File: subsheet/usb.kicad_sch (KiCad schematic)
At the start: 8 parts, among them J501 USB_C_Receptacle, U5 FUSB302BMPX, U501 DT1240A-04LP-7

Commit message: Copy in component arrangement from SDMMC test design
Already had an efficient arrangement for the SPI flash chip, Clock
crystal, and Antenna.
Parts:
- renumbered C708 to C501, C708 to C502, C708 to C503, C708 to C504, C302 to C505, U5 to U502
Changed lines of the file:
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@@
   (symbol (lib_id "power:GND") (at 180.34 45.72 0) (mirror y) (unit 1)
     (in_bom yes) (on_board yes) (dnp no) (fields_autoplaced)
-    (property "Reference" "#PWR019" (at 180.34 52.07 0)
+    (property "Reference" "#PWR0510" (at 180.34 52.07 0)
       (effects (font (size 1.27 1.27)) hide)
     )
@@
   (symbol (lib_id "power:GND") (at 129.54 45.72 0) (mirror y) (unit 1)
     (in_bom yes) (on_board yes) (dnp no) (fields_autoplaced)
-    (property "Reference" "#PWR021" (at 129.54 52.07 0)
+    (property "Reference" "#PWR0505" (at 129.54 52.07 0)
       (effects (font (size 1.27 1.27)) hide)
     )
@@
   (symbol (lib_id "Device:C_Small") (at 129.54 43.18 0) (mirror y) (unit 1)
     (in_bom yes) (on_board yes) (dnp no) (fields_autoplaced)
-    (property "Reference" "C708" (at 132.08 41.9163 0)
+    (property "Reference" "C502" (at 132.08 41.9163 0)
       (effects (font (size 1.27 1.27)) (justify right))
     )
@@
   (symbol (lib_id "power:+5V") (at 180.34 38.1 0) (mirror y) (unit 1)
     (in_bom yes) (on_board yes) (dnp no) (fields_autoplaced)
-    (property "Reference" "#PWR020" (at 180.34 41.91 0)
+    (property "Reference" "#PWR0509" (at 180.34 41.91 0)
       (effects (font (size 1.27 1.27)) hide)
     )
@@
   (symbol (lib_id "Device:C_Small") (at 132.08 68.58 0) (mirror y) (unit 1)
     (in_bom yes) (on_board yes) (dnp no) (fields_autoplaced)
-    (property "Reference" "C708" (at 134.62 67.3163 0)
+    (property "Reference" "C503" (at 134.62 67.3163 0)
       (effects (font (size 1.27 1.27)) (justify right))
     )
@@
   (symbol (lib_id "Device:C_Small") (at 167.64 43.18 0) (mirror y) (unit 1)
     (in_bom yes) (on_board yes) (dnp no) (fields_autoplaced)
-    (property "Reference" "C708" (at 170.18 41.9163 0)
+    (property "Reference" "C504" (at 170.18 41.9163 0)
       (effects (font (size 1.27 1.27)) (justify right))
     )
@@
   (symbol (lib_id "Device:C_Small") (at 180.34 43.18 0) (unit 1)
     (in_bom yes) (on_board yes) (dnp no) (fields_autoplaced)
-    (property "Reference" "C302" (at 182.88 41.9163 0)
+    (property "Reference" "C505" (at 182.88 41.9163 0)
       (effects (font (size 1.27 1.27)) (justify left))
     )
@@
   (symbol (lib_id "power:GND") (at 167.64 45.72 0) (mirror y) (unit 1)
     (in_bom yes) (on_board yes) (dnp no) (fields_autoplaced)
-    (property "Reference" "#PWR019" (at 167.64 52.07 0)
+    (property "Reference" "#PWR0508" (at 167.64 52.07 0)
       (effects (font (size 1.27 1.27)) hide)
     )
@@
   (symbol (lib_id "Device:C_Small") (at 119.38 68.58 0) (mirror y) (unit 1)
     (in_bom yes) (on_board yes) (dnp no) (fields_autoplaced)
-    (property "Reference" "C708" (at 121.92 67.3163 0)
+    (property "Reference" "C501" (at 121.92 67.3163 0)
       (effects (font (size 1.27 1.27)) (justify right))
     )
@@
   (symbol (lib_id "Interface_USB:FUSB302BMPX") (at 152.4 58.42 0) (mirror y) (unit 1)
     (in_bom yes) (on_board yes) (dnp no) (fields_autoplaced)
-    (property "Reference" "U5" (at 152.7459 68.58 0)
-      (effects (font (size 1.27 1.27)) (justify right))
-    )
+    (property "Reference" "U502" (at 152.7459 68.58 0)
+      (effects (font (size 1.27 1.27)) (justify right))
+    )

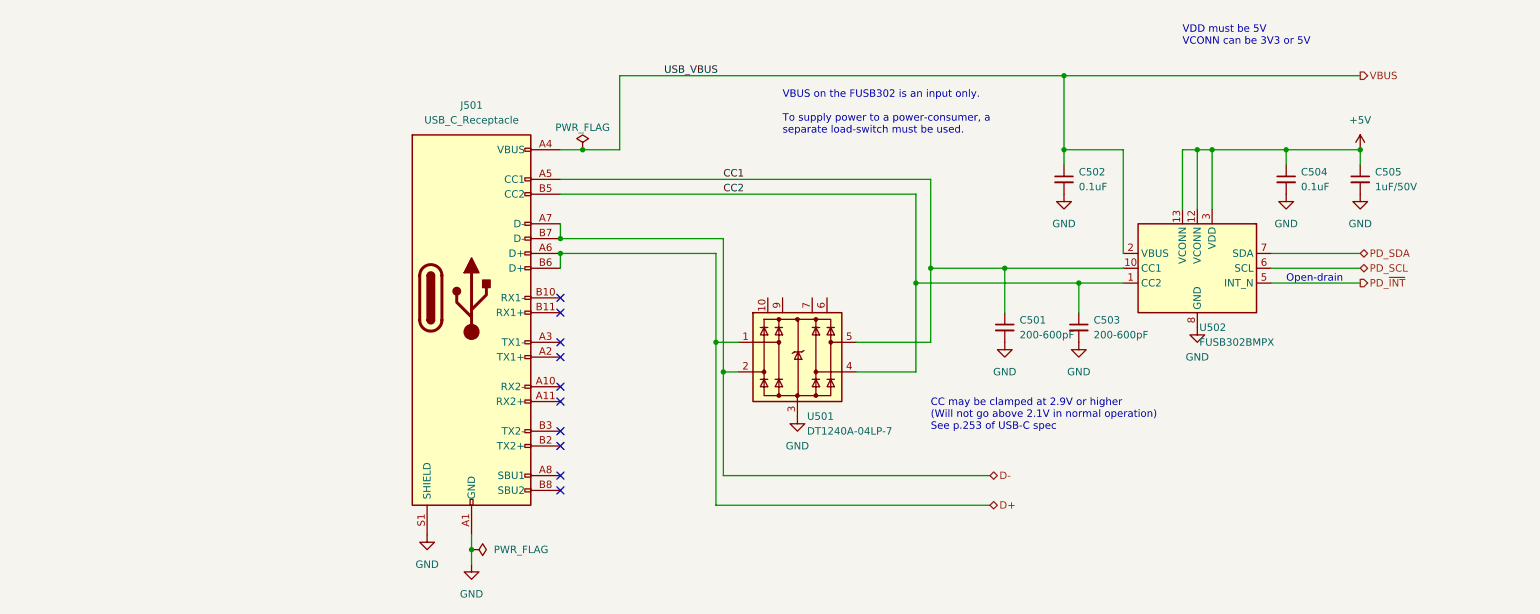
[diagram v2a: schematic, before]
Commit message: Add 5v and 3v3 buck regulators, brige rectifier
Buck regulators are copied from existing designs. 5V regulator needs to
be reworked though; due to ESD vulnerability.

Added 4 diodes in bridge rectifier configuration. Provides a simpler
solution than the polarity-protected eFuse. Due to how the
buck-regulators work, it should be fine for any voltage from ~4.8V 17V
(max Vin of buck regulator). Downside is icnreased power-dissipation,
but since this board is not intended to use a lot of current it should
be good (the USB port can bypass this too, but only for 5V)
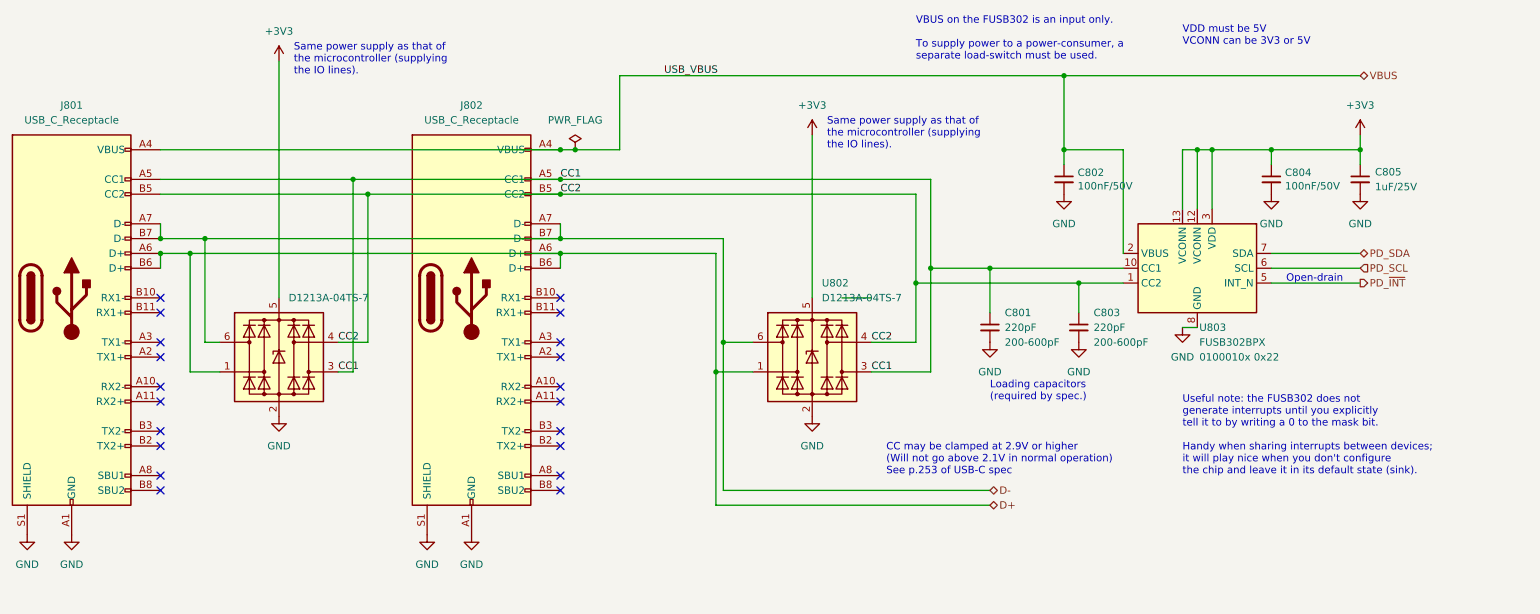
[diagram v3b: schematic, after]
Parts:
- removed C501, C503: 200-600pF, symbol Device:C_Small
- removed C502, C504: 0.1uF, symbol Device:C_Small
- removed C505: 1uF/50V, Capacitor_SMD:C_0805_2012Metric, symbol Device:C_Small
- removed U501: DT1240A-04LP-7, Package_DFN_QFN:Diodes_UDFN-10_1.0x2.5mm_P0.5mm, symbol Power_Protection_custom:DT1240A-04LP-7
- added C801, C803: 220pF, Capacitor_SMD:C_0402_1005Metric, symbol Device:C_Small
- added C802, C804: 100nF/50V, Capacitor_SMD:C_0402_1005Metric, symbol Device:C_Small
- added C805: 1uF/25V, Capacitor_SMD:C_0402_1005Metric, symbol Device:C_Small
- added J801: USB_C_Receptacle, Connector_USB:USB_C_Receptacle_Molex_105450-0101, symbol Connector:USB_C_Receptacle
- added U801, U802: D1213A-04TS-7, Package_TO_SOT_SMD:TSOT-23-6, symbol Power_Protection_custom:D1213A-04TS-7
- U803: renamed from U502; value FUSB302BMPX -> FUSB302BPX; I2C address (none) -> 0100010x 0x22; JLCPCB_CORRECTION (none) -> 0;0;270; LCSC (none) -> C442699
- renumbered J501 to J802
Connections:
- net CC1: now also C801.1, J801.A5 (CC1), U801.3 (I/O2), U802.3 (I/O2)
- net CC2: now also C803.1, J801.B5 (CC2), U801.4 (I/O3), U802.4 (I/O3)
- net D+: now also J801.A6 (D+), J801.B6 (D+), U801.1 (I/O1), U802.1 (I/O1)
- net D-: now also J801.A7 (D-), J801.B7 (D-), U801.6 (I/O4), U802.6 (I/O4)
- net GND: now also C801.2, C802.2, C803.2, C804.2, C805.2, J801.A1 (GND), J801.A12 (GND), J801.B1 (GND), J801.B12 (GND), J801.S1 (SHIELD), U801.2 (GND), U802.2 (GND)
- net VBUS: now also C802.1, J801.A4 (VBUS), J801.A9 (VBUS), J801.B4 (VBUS), J801.B9 (VBUS)
- net +5V renamed +3V3
- net +3V3: now also C804.1, C805.1, U801.5 (VBUS), U802.5 (VBUS)
- no-connect marks 10 -> 20
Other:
- note added: "Loading capacitors (required by spec.)"
- note added: "Same power supply as that of the microcontroller (supplying the IO lines)."
- note added: "Useful note: the FUSB302 does not generate interrupts until you explicitly tell it to by writing a 0 to the mask bit. Handy when sharing interrupts between devices; it will play nice when you don't configure the chip and leave it in its default state (sink)."
- company: (c) Escape This -> copyright Escape This 2024
- title: Environment Controller ESP32-S3-4M -> Puzzle Board

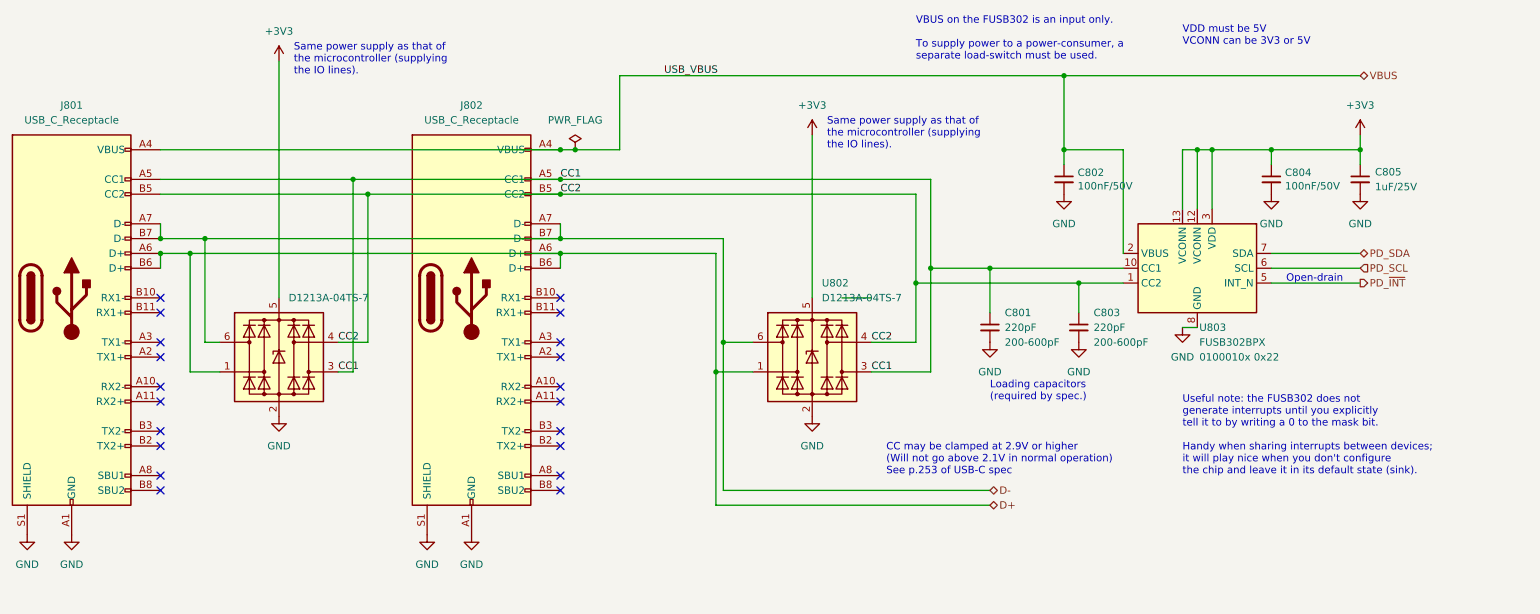
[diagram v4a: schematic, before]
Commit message: Removed USB-PD circuit - simplifies board
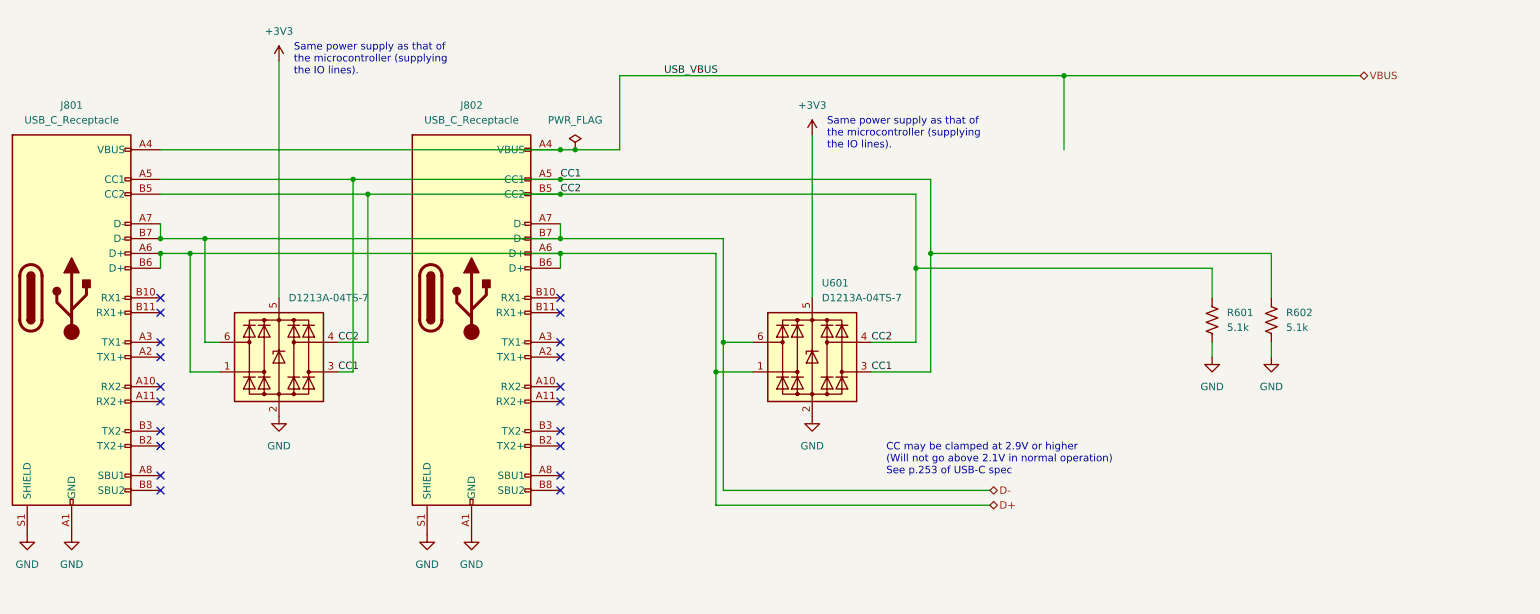
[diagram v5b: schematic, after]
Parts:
- removed C801, C803: 220pF, Capacitor_SMD:C_0402_1005Metric, symbol Device:C_Small
- removed C802, C804: 100nF/50V, Capacitor_SMD:C_0402_1005Metric, symbol Device:C_Small
- removed C805: 1uF/25V, Capacitor_SMD:C_0402_1005Metric, symbol Device:C_Small
- removed U802: D1213A-04TS-7, Package_TO_SOT_SMD:TSOT-23-6, symbol Power_Protection_custom:D1213A-04TS-7
- removed U803: FUSB302BPX, Package_DFN_QFN:WQFN-14-1EP_2.5x2.5mm_P0.5mm_EP1.45x1.45mm, symbol Interface_USB:FUSB302BMPX
- added R601, R602: 5.1k, Resistor_SMD:R_0603_1608Metric, symbol Device:R_US
- added U601: D1213A-04TS-7, Package_TO_SOT_SMD:TSOT-23-6, symbol Power_Protection_custom:D1213A-04TS-7
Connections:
- net +3V3: now also U601.5 (VBUS)
- net CC1: now also R602.2, U601.3 (I/O2)
- net CC2: now also R601.2, U601.4 (I/O3)
- net D+: now also U601.1 (I/O1)
- net D-: now also U601.6 (I/O4)
- net GND: now also R601.1, R602.1, U601.2 (GND)
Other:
- note removed: "Loading capacitors (required by spec.)"
- note removed: "Open-drain"
- note removed: "Useful note: the FUSB302 does not generate interrupts until you explicitly tell it to by writing a 0 to the mask bit. Handy when sharing interrupts between devices; it will play nice when you don't configure the chip and leave it in its default state (sink)."
- note removed: "VBUS on the FUSB302 is an input only. To supply power to a power-consumer, a separate load-switch must be used."
- note removed: "VDD must be 5V VCONN can be 3V3 or 5V"

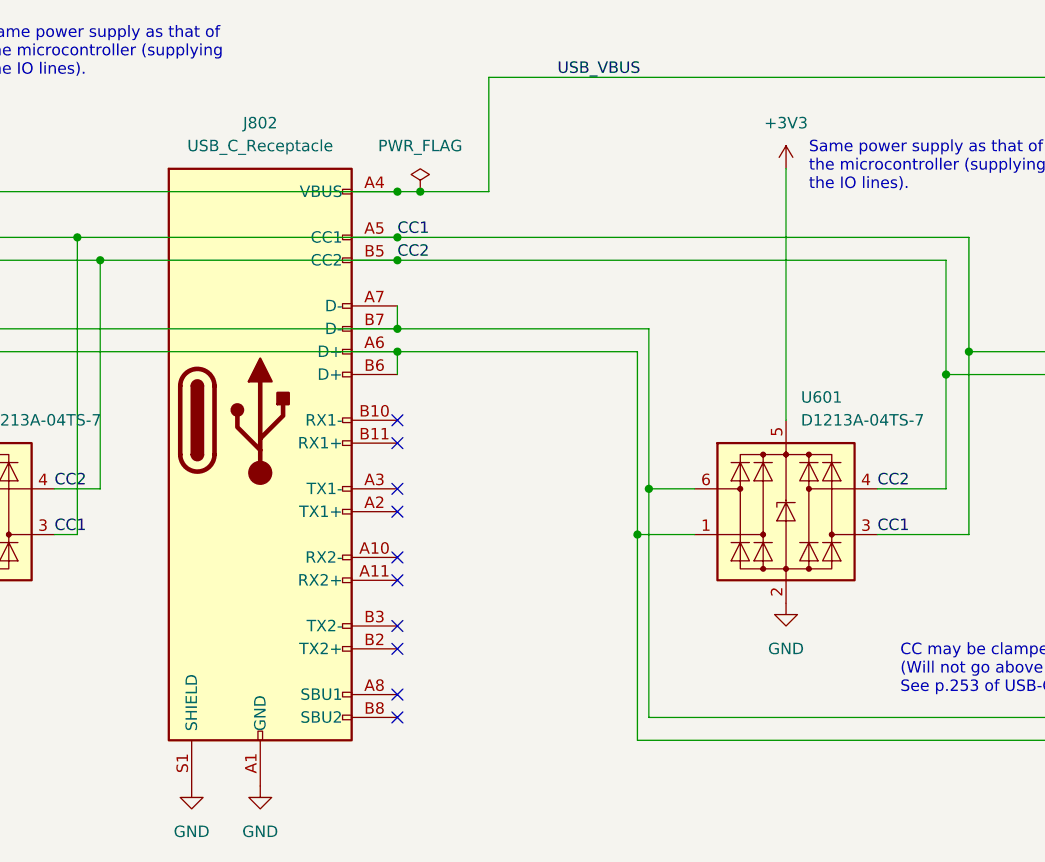
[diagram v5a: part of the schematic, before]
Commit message: Position final few components
Removed one ESD diode arrray - experimental board, so not really needed,
with the exception of the USB lines.

Add and position 5V indicator LED

Finished wiring up the 5V buck-boost regulator
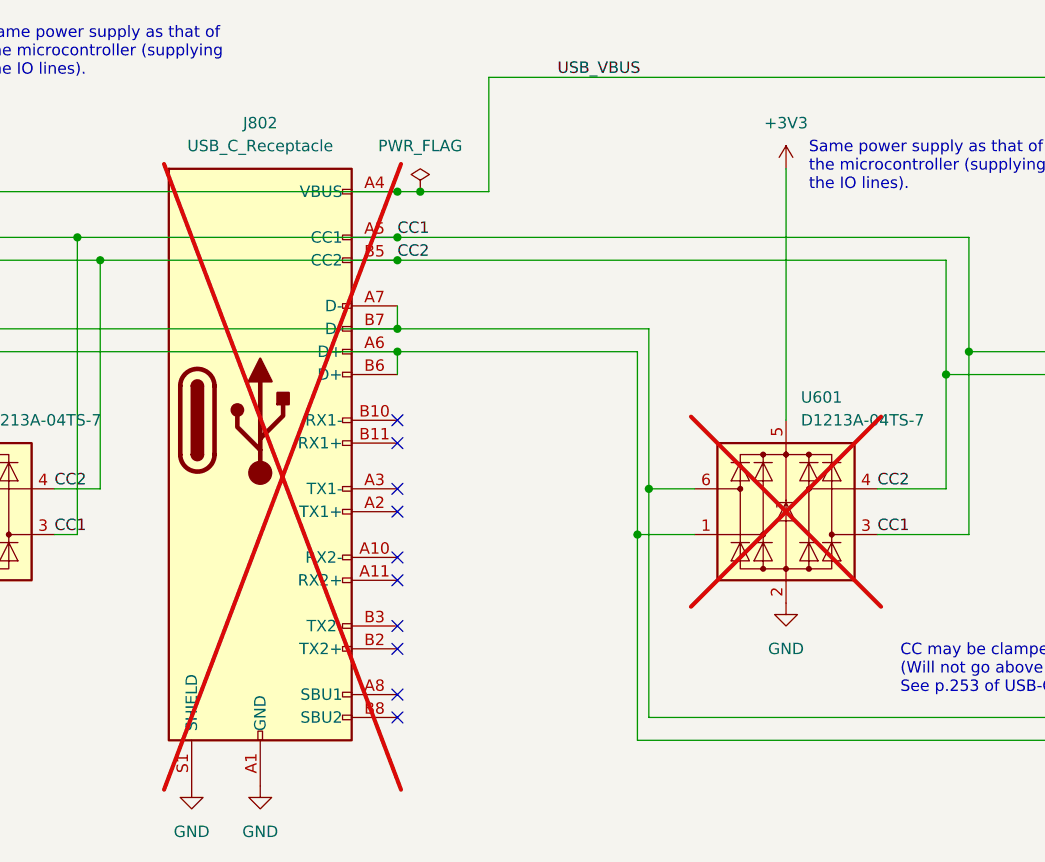
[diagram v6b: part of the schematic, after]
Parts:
- J802, U601: now not fitted; now left out of the parts list

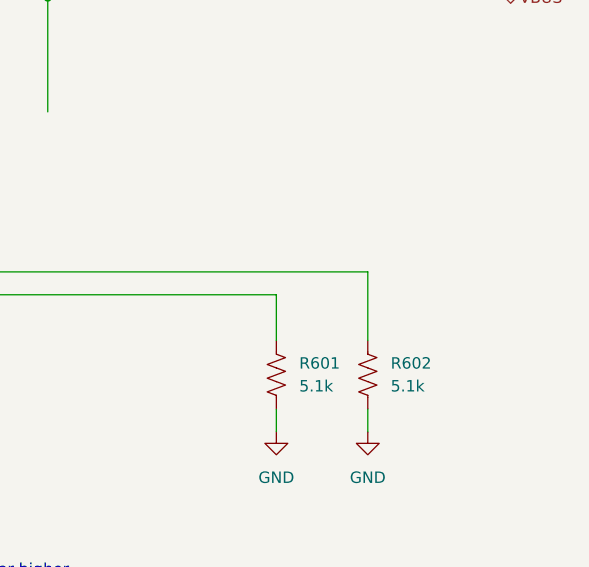
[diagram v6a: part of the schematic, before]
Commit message: Wire remaining traces, fix DRC errors
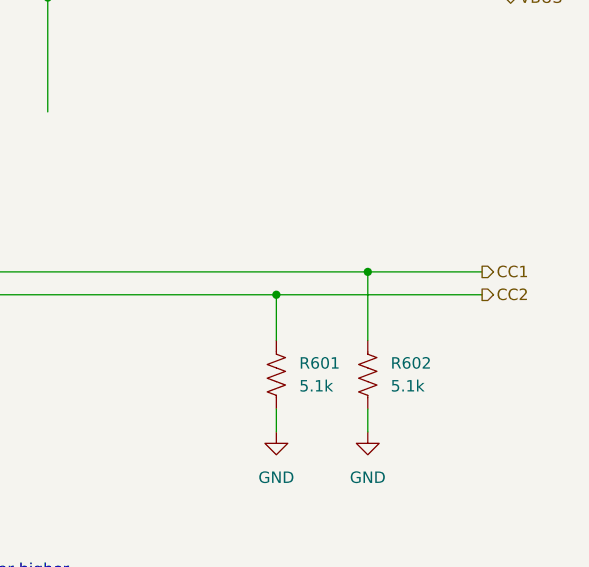
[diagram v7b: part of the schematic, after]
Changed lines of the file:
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@@
+	)
+	(junction
+		(at 154.94 58.42)
+		(diameter 0)
+		(color 0 0 0 0)
 	)
 	(junction
@@
 	)
 	(junction
+		(at 165.1 55.88)
+		(diameter 0)
+		(color 0 0 0 0)
+	)
+	(junction
 		(at -20.32 55.88)
 		(diameter 0)
@@
 	(wire
 		(pts
+			(xy 165.1 55.88) (xy 177.8 55.88)
+		)
+		(stroke
+			(width 0)
+			(type default)
+		)
+	)
+	(wire
+		(pts
 			(xy 53.34 38.1) (xy 53.34 25.4)
 		)
@@
 		(pts
 			(xy 129.54 25.4) (xy 129.54 38.1)
+		)
+		(stroke
+			(width 0)
+			(type default)
+		)
+	)
+	(wire
+		(pts
+			(xy 154.94 58.42) (xy 177.8 58.42)
 		)
 		(stroke
@@
 		(fields_autoplaced yes)
 		(effects
+			(font
+				(size 1.27 1.27)
+			)
+			(justify left)
+		)
+	)
+	(hierarchical_label "CC1"
+		(shape output)
+		(at 177.8 55.88 0)
+		(fields_autoplaced yes)
+		(effects
+			(font
+				(size 1.27 1.27)
+			)
+			(justify left)
+		)
+	)
+	(hierarchical_label "CC2"
+		(shape output)
+		(at 177.8 58.42 0)
+		(fields_autoplaced yes)
+		(effects
